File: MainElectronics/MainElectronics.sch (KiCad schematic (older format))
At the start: 2 parts

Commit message: Forgot to save schematic
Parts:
- added BT?: Battery, symbol Device:Battery
- added SW?: SW_E_STOP, symbol Switch:SW_SPST
- added U?: RFM95W_Adafruit_Breakout, symbol MainElectronicsLib:RFM95W_Adafruit_Breakout
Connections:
- new net: BT?.1 (+), SW?.2 (B)
- new net +BATT: SW?.1 (A)
- new net -BATT: BT?.2 (-)
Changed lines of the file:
@@
+	1    0    0    -1
+$EndComp
+$Comp
+L power:+BATT #PWR?
+U 1 1 5ED83A12
+P 9950 1300
+F 0 "#PWR?" H 9950 1150 50  0001 C CNN
+F 1 "+BATT" H 9900 1450 50  0000 C CNN
+F 2 "" H 9950 1300 50  0001 C CNN
+F 3 "" H 9950 1300 50  0001 C CNN
+	1    9950 1300
+	1    0    0    -1
+$EndComp
+$Comp
+L power:-BATT #PWR?
+U 1 1 5ED83D2D
+P 10350 1700
+F 0 "#PWR?" H 10350 1550 50  0001 C CNN
+F 1 "-BATT" H 10365 1873 50  0000 C CNN
+F 2 "" H 10350 1700 50  0001 C CNN
+F 3 "" H 10350 1700 50  0001 C CNN
+	1    10350 1700
+	-1   0    0    1
+$EndComp
+$Comp
+L Device:Battery BT?
+U 1 1 5ED842D7
+P 10350 1500
+F 0 "BT?" H 10458 1546 50  0000 L CNN
+F 1 "Battery" H 10458 1455 50  0000 L CNN
+F 2 "" V 10350 1560 50  0001 C CNN
+F 3 "~" V 10350 1560 50  0001 C CNN
+	1    10350 1500
+	1    0    0    -1
+$EndComp
+$Comp
+L Switch:SW_SPST SW?
+U 1 1 5ED8AA7B
+P 10150 1300
+F 0 "SW?" H 10100 1400 50  0000 C CNN
+F 1 "SW_E_STOP" H 10450 1400 50  0000 C CNN
+F 2 "" H 10150 1300 50  0001 C CNN
+F 3 "~" H 10150 1300 50  0001 C CNN
+	1    10150 1300
+	1    0    0    -1
+$EndComp
+$Comp
+L MainElectronicsLib:RFM95W_Adafruit_Breakout U?
+U 1 1 5ED8CB9C
+P 5350 8550
+F 0 "U?" H 5325 9215 50  0000 C CNN
+F 1 "RFM95W_Adafruit_Breakout" H 5325 9124 50  0000 C CNN
+F 2 "" H 5350 8550 50  0001 C CNN
+F 3 "" H 5350 8550 50  0001 C CNN
+	1    5350 8550
 	1    0    0    -1
 $EndComp

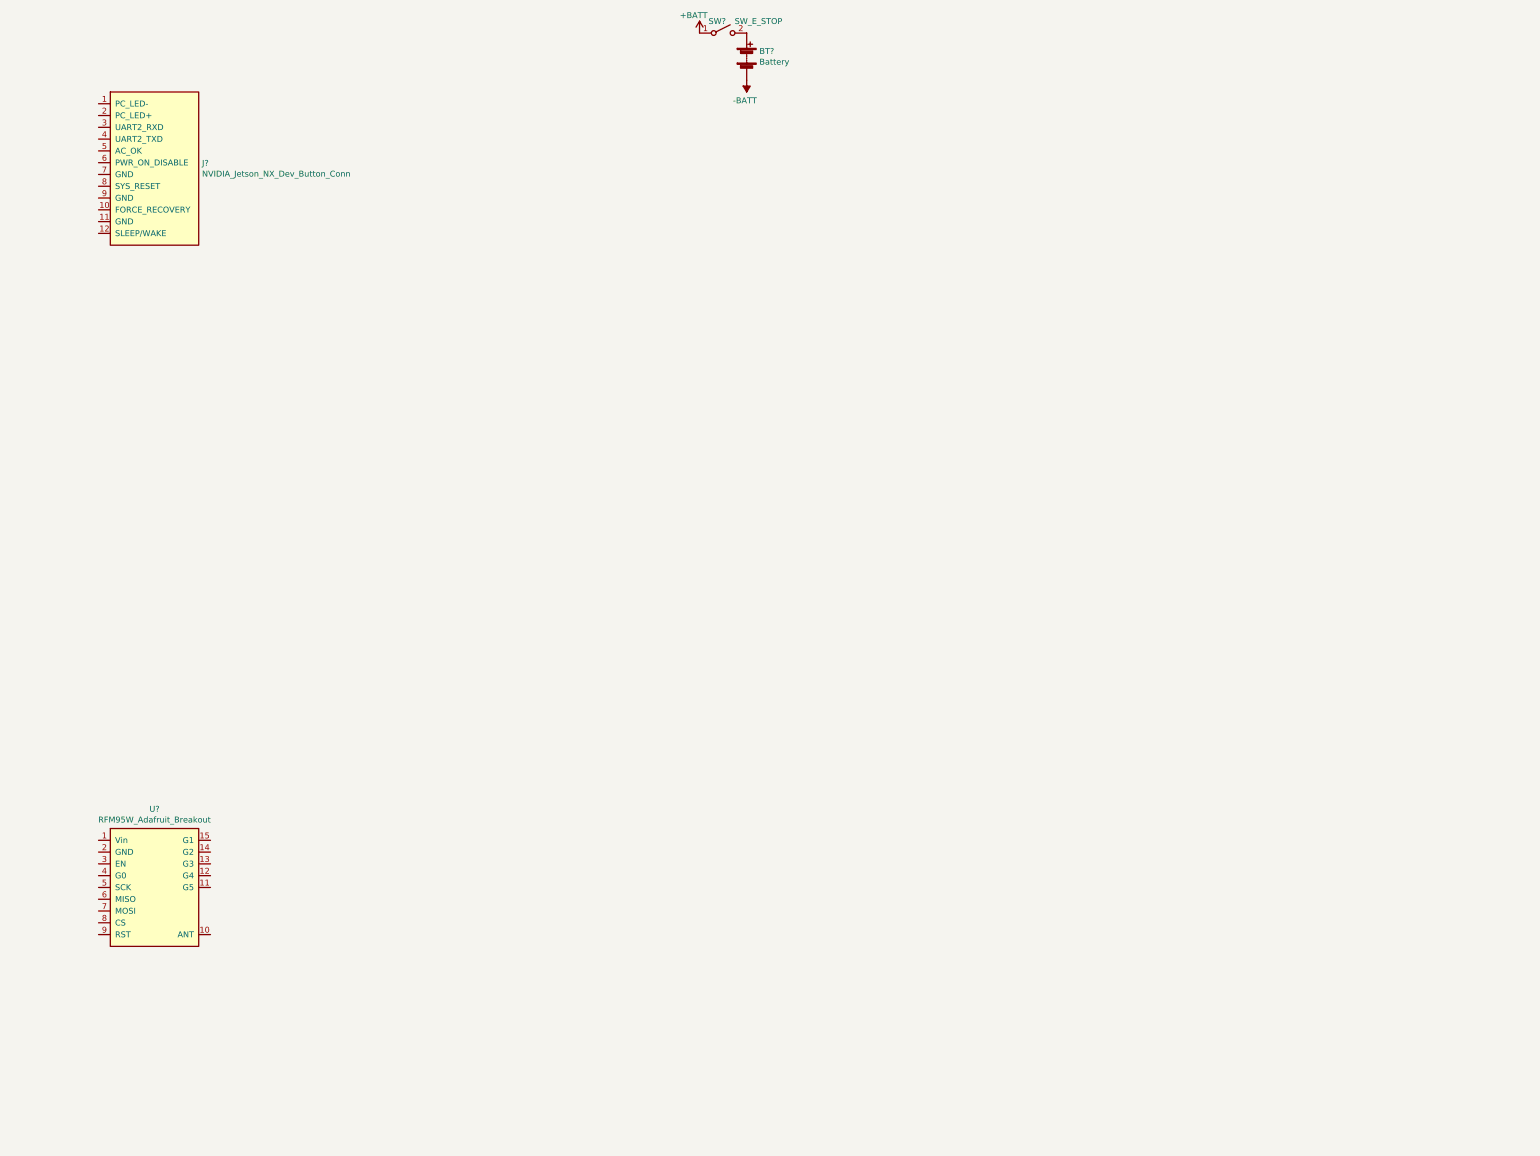
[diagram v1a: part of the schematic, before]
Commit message: Added schematic symbols to schematic
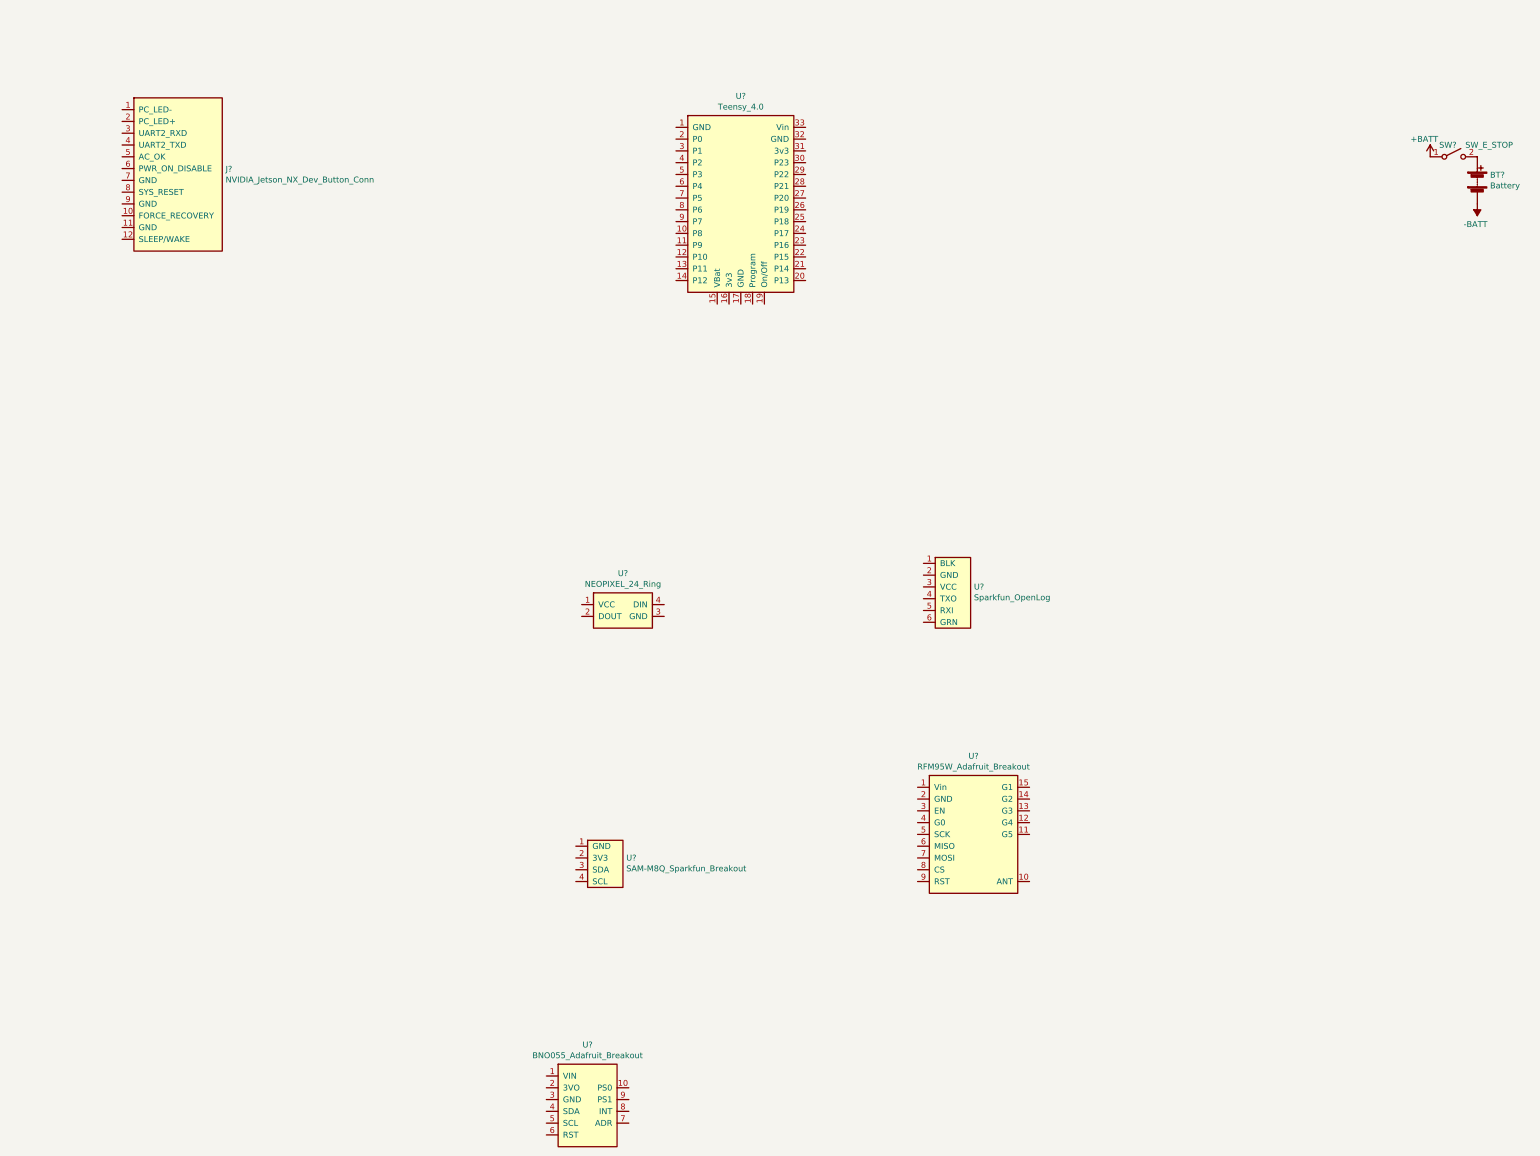
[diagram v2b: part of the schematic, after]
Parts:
- added U?: BNO055_Adafruit_Breakout, symbol MainElectronicsLib:BNO055_Adafruit_Breakout
- added U?: NEOPIXEL_24_Ring, symbol MainElectronicsLib:NEOPIXEL_24_Ring
- added U?: SAM-M8Q_Sparkfun_Breakout, symbol MainElectronicsLib:SAM-M8Q_Sparkfun_Breakout
- added U?: Sparkfun_OpenLog, symbol MainElectronicsLib:Sparkfun_OpenLog
- added U?: Teensy_4.0, symbol MainElectronicsLib:Teensy_4.0
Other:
- moved on the sheet: BT?, J?, SW?, U?
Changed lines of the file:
@@
 L MainElectronicsLib:NVIDIA_Jetson_NX_Dev_Button_Conn J?
 U 1 1 5ED74642
-P 5300 2700
-F 0 "J?" H 5728 2996 50  0000 L CNN
-F 1 "NVIDIA_Jetson_NX_Dev_Button_Conn" H 5728 2905 50  0000 L CNN
-F 2 "" H 5300 3650 50  0001 C CNN
-F 3 "" H 5300 3650 50  0001 C CNN
-	1    5300 2700
+P 5500 2750
+F 0 "J?" H 5928 3046 50  0000 L CNN
+F 1 "NVIDIA_Jetson_NX_Dev_Button_Conn" H 5928 2955 50  0000 L CNN
+F 2 "" H 5500 3700 50  0001 C CNN
+F 3 "" H 5500 3700 50  0001 C CNN
+	1    5500 2750
 	1    0    0    -1
 $EndComp
@@
 L power:+BATT #PWR?
 U 1 1 5ED83A12
-P 9950 1300
-F 0 "#PWR?" H 9950 1150 50  0001 C CNN
-F 1 "+BATT" H 9900 1450 50  0000 C CNN
-F 2 "" H 9950 1300 50  0001 C CNN
-F 3 "" H 9950 1300 50  0001 C CNN
-	1    9950 1300
+P 16150 2350
+F 0 "#PWR?" H 16150 2200 50  0001 C CNN
+F 1 "+BATT" H 16100 2500 50  0000 C CNN
+F 2 "" H 16150 2350 50  0001 C CNN
+F 3 "" H 16150 2350 50  0001 C CNN
+	1    16150 2350
 	1    0    0    -1
 $EndComp
@@
 L power:-BATT #PWR?
 U 1 1 5ED83D2D
-P 10350 1700
-F 0 "#PWR?" H 10350 1550 50  0001 C CNN
-F 1 "-BATT" H 10365 1873 50  0000 C CNN
-F 2 "" H 10350 1700 50  0001 C CNN
-F 3 "" H 10350 1700 50  0001 C CNN
-	1    10350 1700
+P 16550 2750
+F 0 "#PWR?" H 16550 2600 50  0001 C CNN
+F 1 "-BATT" H 16565 2923 50  0000 C CNN
+F 2 "" H 16550 2750 50  0001 C CNN
+F 3 "" H 16550 2750 50  0001 C CNN
+	1    16550 2750
 	-1   0    0    1
 $EndComp
@@
 L Device:Battery BT?
 U 1 1 5ED842D7
-P 10350 1500
-F 0 "BT?" H 10458 1546 50  0000 L CNN
-F 1 "Battery" H 10458 1455 50  0000 L CNN
-F 2 "" V 10350 1560 50  0001 C CNN
-F 3 "~" V 10350 1560 50  0001 C CNN
-	1    10350 1500
+P 16550 2550
+F 0 "BT?" H 16658 2596 50  0000 L CNN
+F 1 "Battery" H 16658 2505 50  0000 L CNN
+F 2 "" V 16550 2610 50  0001 C CNN
+F 3 "~" V 16550 2610 50  0001 C CNN
+	1    16550 2550
 	1    0    0    -1
 $EndComp
@@
 L Switch:SW_SPST SW?
 U 1 1 5ED8AA7B
-P 10150 1300
-F 0 "SW?" H 10100 1400 50  0000 C CNN
-F 1 "SW_E_STOP" H 10450 1400 50  0000 C CNN
-F 2 "" H 10150 1300 50  0001 C CNN
-F 3 "~" H 10150 1300 50  0001 C CNN
-	1    10150 1300
+P 16350 2350
+F 0 "SW?" H 16300 2450 50  0000 C CNN
+F 1 "SW_E_STOP" H 16650 2450 50  0000 C CNN
+F 2 "" H 16350 2350 50  0001 C CNN
+F 3 "~" H 16350 2350 50  0001 C CNN
+	1    16350 2350
 	1    0    0    -1
 $EndComp
@@
 L MainElectronicsLib:RFM95W_Adafruit_Breakout U?
 U 1 1 5ED8CB9C
-P 5350 8550
-F 0 "U?" H 5325 9215 50  0000 C CNN
-F 1 "RFM95W_Adafruit_Breakout" H 5325 9124 50  0000 C CNN
-F 2 "" H 5350 8550 50  0001 C CNN
-F 3 "" H 5350 8550 50  0001 C CNN
-	1    5350 8550
+P 12300 8100
+F 0 "U?" H 12275 8765 50  0000 C CNN
+F 1 "RFM95W_Adafruit_Breakout" H 12275 8674 50  0000 C CNN
+F 2 "" H 12300 8100 50  0001 C CNN
+F 3 "" H 12300 8100 50  0001 C CNN
+	1    12300 8100
 	1    0    0    -1
 $EndComp
+$Comp
+L MainElectronicsLib:BNO055_Adafruit_Breakout U?
+U 1 1 5EDC2630
+P 9000 10400
+F 0 "U?" H 9000 10915 50  0000 C CNN
+F 1 "BNO055_Adafruit_Breakout" H 9000 10824 50  0000 C CNN
+F 2 "" H 9000 10200 50  0001 C CNN
+F 3 "" H 9000 10200 50  0001 C CNN
+	1    9000 10400
+	1    0    0    -1
+$EndComp
+$Comp
+L MainElectronicsLib:NEOPIXEL_24_Ring U?
+U 1 1 5EDC2F01
+P 9300 6200
+F 0 "U?" H 9300 6515 50  0000 C CNN
+F 1 "NEOPIXEL_24_Ring" H 9300 6424 50  0000 C CNN
+F 2 "" H 9300 6200 50  0001 C CNN
+F 3 "" H 9300 6200 50  0001 C CNN
+	1    9300 6200
+	1    0    0    -1
+$EndComp
+$Comp
+L MainElectronicsLib:SAM-M8Q_Sparkfun_Breakout U?
+U 1 1 5EDC31DA
+P 9150 8400
+F 0 "U?" H 9328 8501 50  0000 L CNN
+F 1 "SAM-M8Q_Sparkfun_Breakout" H 9328 8410 50  0000 L CNN
+F 2 "" H 9150 8400 50  0001 C CNN
+F 3 "" H 9150 8400 50  0001 C CNN
+	1    9150 8400
+	1    0    0    -1
+$EndComp
+$Comp
+L MainElectronicsLib:Sparkfun_OpenLog U?
+U 1 1 5EDC373B
+P 12100 6050
+F 0 "U?" H 12278 6101 50  0000 L CNN
+F 1 "Sparkfun_OpenLog" H 12278 6010 50  0000 L CNN
+F 2 "" H 12100 6050 50  0001 C CNN
+F 3 "" H 12100 6050 50  0001 C CNN
+	1    12100 6050
+	1    0    0    -1
+$EndComp
+$Comp
+L MainElectronicsLib:Teensy_4.0 U?
+U 1 1 5EDC3CB9
+P 10300 2750
+F 0 "U?" H 10300 3665 50  0000 C CNN
+F 1 "Teensy_4.0" H 10300 3574 50  0000 C CNN
+F 2 "" H 10300 2750 50  0001 C CNN
+F 3 "" H 10300 2750 50  0001 C CNN
+	1    10300 2750
+	1    0    0    -1
+$EndComp

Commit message: Connected components to power
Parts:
- added J?: Jetson_DC_In, symbol Connector_Generic:Conn_01x02
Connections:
- net +BATT: now also J?.2 (Pin_2)
- net -BATT: now also J?.1 (Pin_1)
- net GND: now reaches J?.14 (GND)
- net GND: now also J?.11 (GND), J?.20 (GND), J?.25 (GND), J?.30 (GND), J?.34 (GND), J?.39 (GND), J?.6 (GND), J?.7 (GND), J?.9 (GND), J?.9 (GND), U?.1 (BLK), U?.1 (GND), U?.1 (GND), U?.17 (GND), U?.2 (GND), U?.2 (GND), U?.3 (GND), U?.3 (GND), U?.32 (GND)
- net +5V: now reaches J?.2 (5v)
- net +5V: now also J?.4 (5v), U?.1 (VCC), U?.33 (Vin)
- net +3V3: now reaches U?.1 (Vin)
- net +3V3: now also U?.1 (VIN), U?.16 (3v3), U?.2 (3V3), U?.3 (VCC)
- no-connect marks 0 -> 2

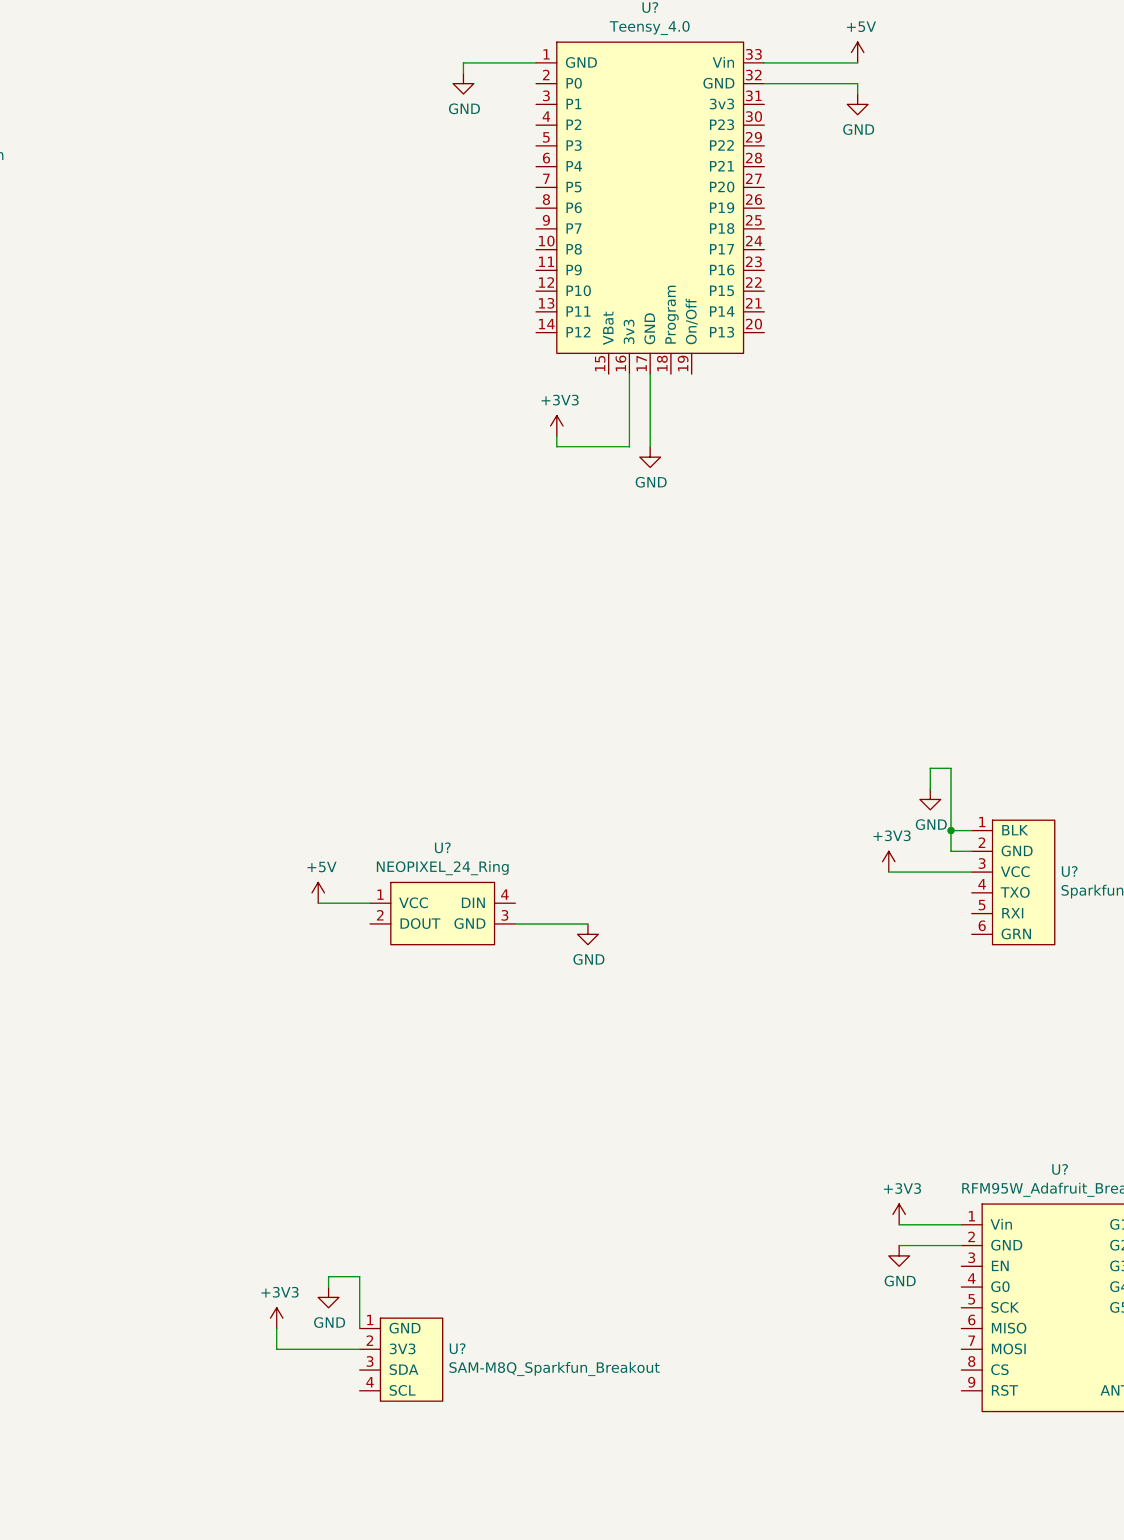
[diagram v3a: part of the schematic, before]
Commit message: Connected OpenLog, Neopixel, and GPS
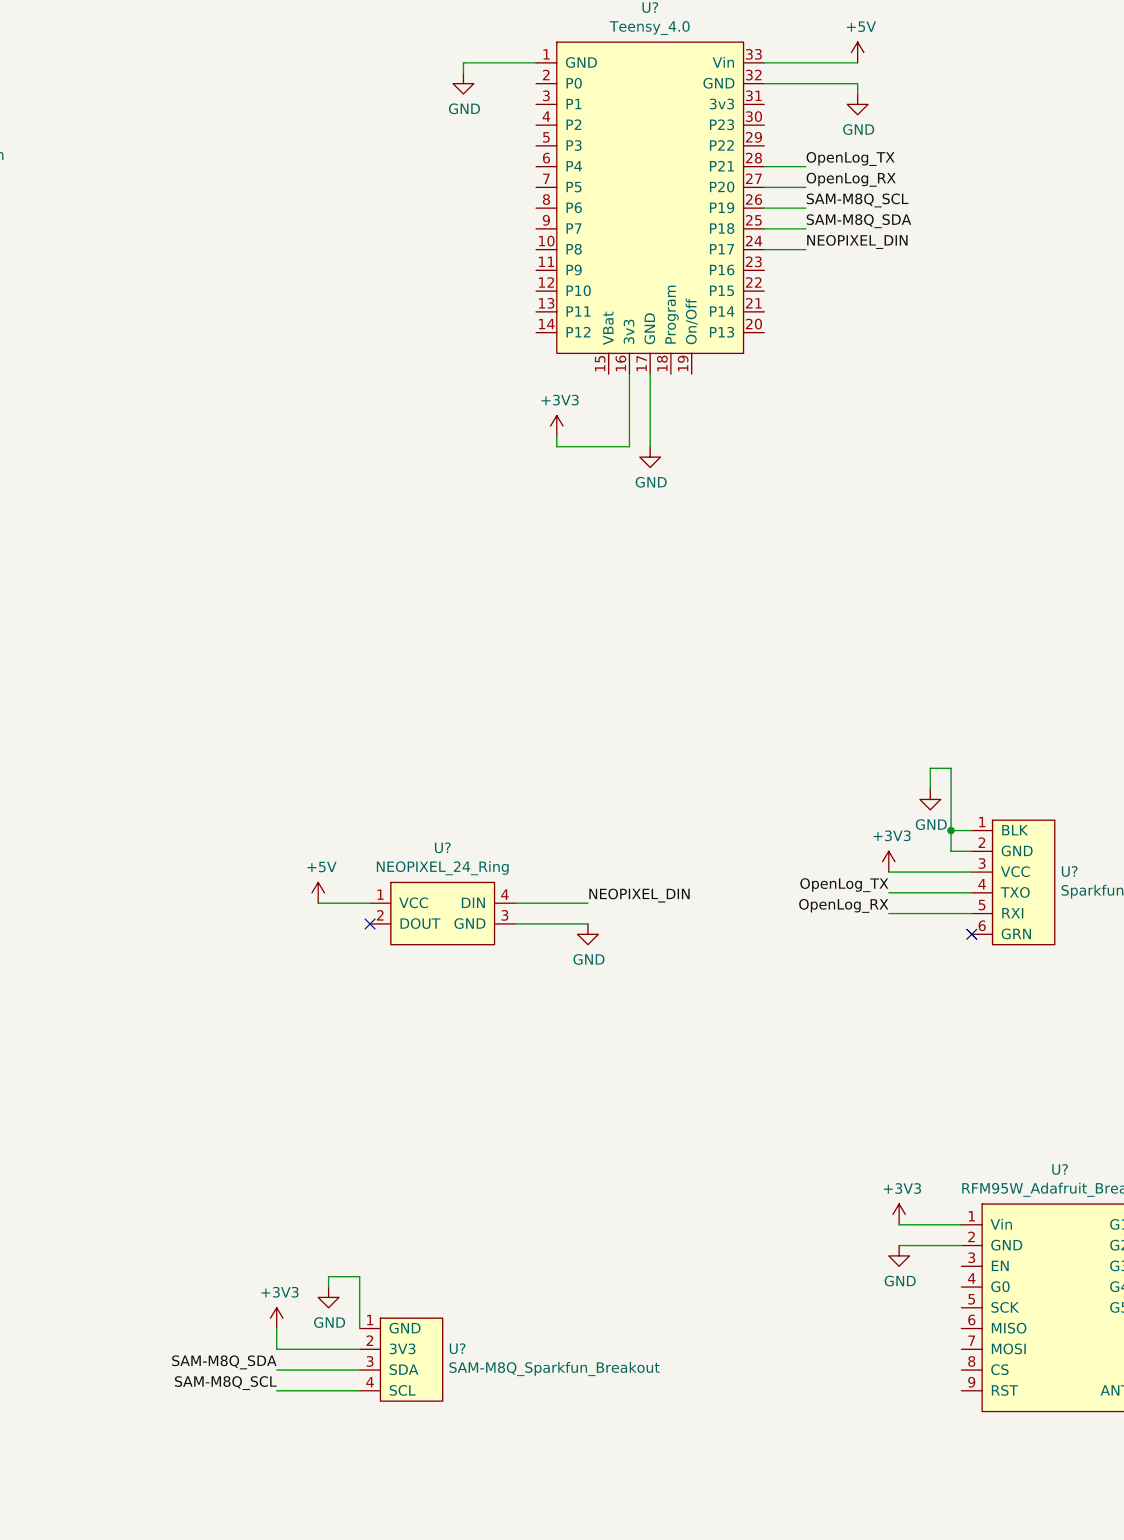
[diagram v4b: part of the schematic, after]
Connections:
- net NEOPIXEL_DIN: now reaches U?.4 (DIN)
- net NEOPIXEL_DIN: now also U?.24 (P17)
- net SAM-M8Q_SDA: now reaches U?.3 (SDA)
- net SAM-M8Q_SDA: now also U?.25 (P18)
- net SAM-M8Q_SCL: now reaches U?.4 (SCL)
- net SAM-M8Q_SCL: now also U?.26 (P19)
- net OpenLog_TX: now reaches U?.4 (TXO)
- net OpenLog_TX: now also U?.28 (P21)
- net OpenLog_RX: now reaches U?.5 (RXI)
- net OpenLog_RX: now also U?.27 (P20)
- no-connect marks 2 -> 4
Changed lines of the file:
@@
 Wire Wire Line
 	8650 10350 8300 10350
+Wire Wire Line
+	11850 6100 11450 6100
+Wire Wire Line
+	11850 6200 11450 6200
+Text Label 11450 6100 2    50   ~ 0
+OpenLog_TX
+Text Label 11450 6200 2    50   ~ 0
+OpenLog_RX
+Text Label 11050 2600 0    50   ~ 0
+OpenLog_TX
+Wire Wire Line
+	11050 2600 10850 2600
+Wire Wire Line
+	10850 2700 11050 2700
+Text Label 11050 2700 0    50   ~ 0
+OpenLog_RX
+Wire Wire Line
+	8900 8400 8500 8400
+Wire Wire Line
+	8900 8500 8500 8500
+Text Label 8500 8400 2    50   ~ 0
+SAM-M8Q_SDA
+Text Label 8500 8500 2    50   ~ 0
+SAM-M8Q_SCL
+Text Label 11050 2900 0    50   ~ 0
+SAM-M8Q_SDA
+Text Label 11050 2800 0    50   ~ 0
+SAM-M8Q_SCL
+Wire Wire Line
+	11050 2800 10850 2800
+Wire Wire Line
+	11050 2900 10850 2900
+NoConn ~ 11850 6300
+NoConn ~ 8950 6250
+Wire Wire Line
+	9650 6150 10000 6150
+Text Label 10000 6150 0    50   ~ 0
+NEOPIXEL_DIN
+Wire Wire Line
+	10850 3000 11050 3000
+Text Label 11050 3000 0    50   ~ 0
+NEOPIXEL_DIN
 $EndSCHEMATC
